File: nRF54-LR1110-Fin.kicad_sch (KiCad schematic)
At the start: 15 parts, among them U1 LR1110IMLTRT, U2 SKY13380-350LF, Y1 TG2520SMN 32.0000M-MCGNNM3, Y2 32.768KHz

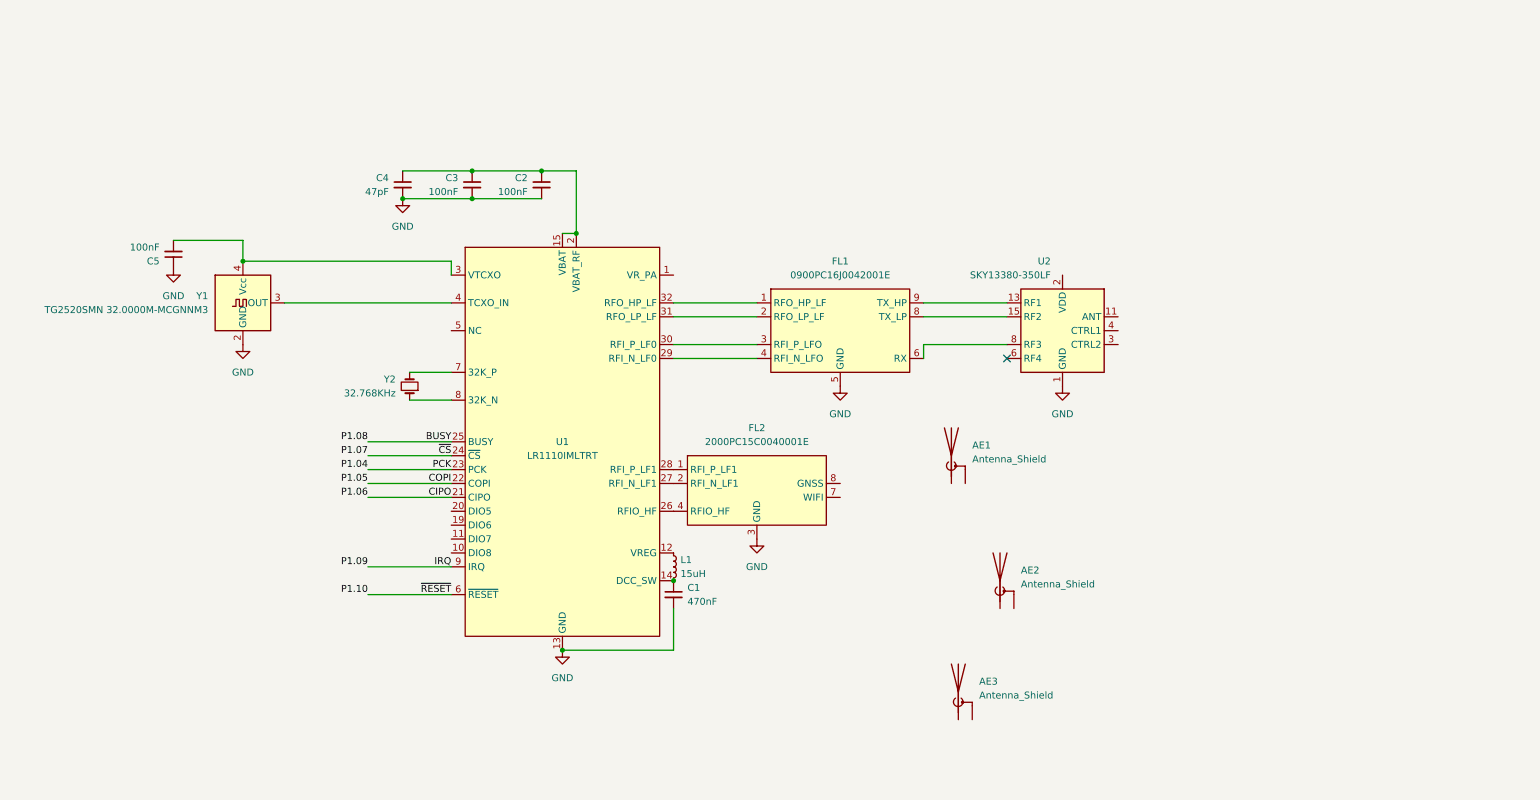
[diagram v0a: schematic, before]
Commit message: schematic: add level shifter, gnss amp
Adds level shifter to L15-DK, GNSS amplifier, proper handling of RF
components for LoRA radio, initial board outline.

Signed-off-by: Helmut Lord <kellyhlord@gmail.com>
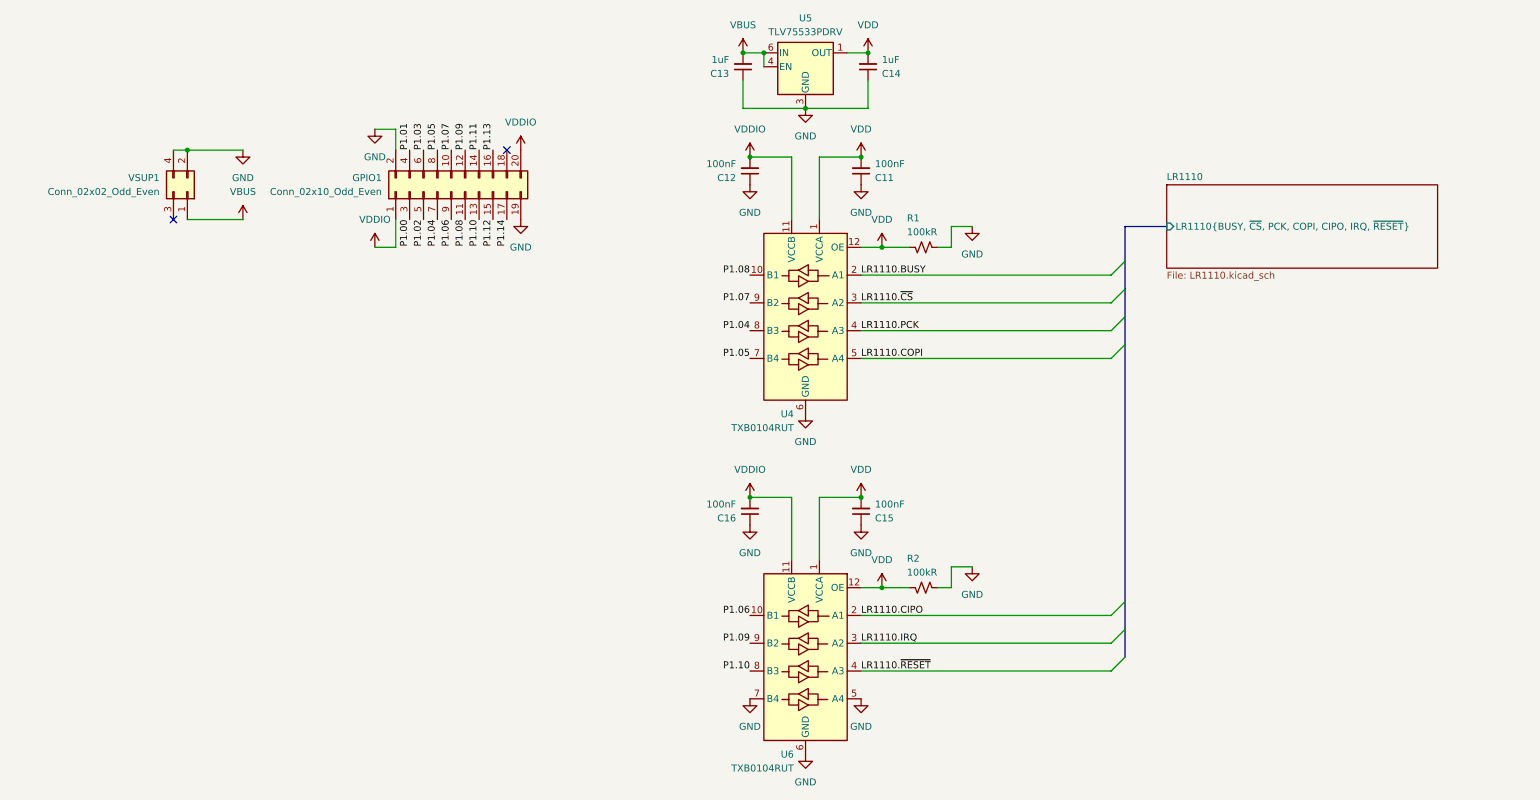
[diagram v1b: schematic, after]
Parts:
- removed AE1, AE2, AE3: Antenna_Shield, Connector_Coaxial:SMA_Amphenol_132289_EdgeMount, symbol Device:Antenna_Shield
- removed C1: 470nF, symbol Device:C_Small
- removed C2, C3, C5: 100nF, symbol Device:C_Small
- removed C4: 47pF, symbol Device:C_Small
- removed FL1: 0900PC16J0042001E, RF_Converter:Balun_Johanson_0900FM15K0039, symbol nRF54-LR1110-Fin-RF:0900PC16J0042001E
- removed FL2: 2000PC15C0040001E, RF_Converter:Balun_Johanson_0900FM15K0039, symbol nRF54-LR1110-Fin-RF:2000PC15C0040001E
- removed L1: 15uH, symbol Device:L_Small
- removed U1: LR1110IMLTRT, Package_DFN_QFN:QFN-32-1EP_5x5mm_P0.5mm_EP3.7x3.7mm_ThermalVias, symbol nRF54-LR1110-Fin-RF:LR1110IMLTRT
- removed U2: SKY13380-350LF, Package_DFN_QFN:QFN-16-1EP_3x3mm_P0.5mm_EP1.7x1.7mm, symbol RF_Switch:SKY13380-350LF
- removed Y1: TG2520SMN 32.0000M-MCGNNM3, Oscillator:Oscillator_SMD_SeikoEpson_TG2520SMN-xxx-xxxxxx-4Pin_2.5x2.0mm, symbol Oscillator:TG2520SMN-xx.xxxxxxMhz-xxxxNM
- removed Y2: 32.768KHz, symbol Device:Crystal_Small
- added C11, C12, C15, C16: 100nF, Capacitor_SMD:C_0402_1005Metric, symbol Device:C_Small
- added C13, C14: 1uF, Capacitor_SMD:C_0402_1005Metric, symbol Device:C_Small
- added GPIO1: Conn_02x10_Odd_Even, Connector_PinSocket_2.54mm:PinSocket_2x10_P2.54mm_Horizontal, symbol Connector_Generic:Conn_02x10_Odd_Even
- added R1, R2: 100kR, Resistor_SMD:R_0402_1005Metric, symbol Device:R_Small_US
- added U4, U6: TXB0104RUT, Package_DFN_QFN:Texas_R-PUQFN-N12, symbol Logic_LevelTranslator:TXB0104RUT
- added U5: TLV75533PDRV, Package_SON:WSON-6-1EP_2x2mm_P0.65mm_EP1x1.6mm_ThermalVias, symbol Regulator_Linear:TLV75533PDRV
- added VSUP1: Conn_02x02_Odd_Even, Connector_PinSocket_2.54mm:PinSocket_2x02_P2.54mm_Horizontal, symbol Connector_Generic:Conn_02x02_Odd_Even
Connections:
- net GND: now also C11.1, C12.1, C13.1, C14.1, C15.1, C16.1, GPIO1.19 (Pin_19), GPIO1.2 (Pin_2), R1.2, R2.2, U4.6 (GND), U5.3 (GND), U5.7 (GND), U6.5 (A4), U6.6 (GND), U6.7 (B4), VSUP1.2 (Pin_2), VSUP1.4 (Pin_4)
- net P1.04: now also GPIO1.7 (Pin_7), U4.8 (B3)
- net P1.07: now also GPIO1.10 (Pin_10), U4.9 (B2)
- net P1.10: now also GPIO1.13 (Pin_13), U6.8 (B3)
- new net LR1110.BUSY: U4.2 (A1)
- new net LR1110.CIPO: U6.2 (A1)
- new net LR1110.COPI: U4.5 (A4)
- new net LR1110.IRQ: U6.3 (A2)
- new net LR1110.PCK: U4.4 (A3)
- new net LR1110.~{CS}: U4.3 (A2)
- new net LR1110.~{RESET}: U6.4 (A3)
- new net P1.00: GPIO1.3 (Pin_3)
- new net P1.01: GPIO1.4 (Pin_4)
- new net P1.02: GPIO1.5 (Pin_5)
- new net P1.03: GPIO1.6 (Pin_6)
- new net P1.05: GPIO1.8 (Pin_8), U4.7 (B4)
- new net P1.06: GPIO1.9 (Pin_9), U6.10 (B1)
- new net P1.08: GPIO1.11 (Pin_11), U4.10 (B1)
- new net P1.09: GPIO1.12 (Pin_12), U6.9 (B2)
- new net P1.11: GPIO1.14 (Pin_14)
- new net P1.12: GPIO1.15 (Pin_15)
- new net P1.13: GPIO1.16 (Pin_16)
- new net P1.14: GPIO1.17 (Pin_17)
- new net VBUS: C13.2, U5.4 (EN), U5.6 (IN), VSUP1.1 (Pin_1)
- new net VDD: C11.2, C14.2, C15.2, R1.1, R2.1, U4.1 (VCCA), U4.12 (OE), U5.1 (OUT), U6.1 (VCCA), U6.12 (OE)
- new net VDDIO: C12.2, C16.2, GPIO1.1 (Pin_1), GPIO1.20 (Pin_20), U4.11 (VCCB), U6.11 (VCCB)
- no-connect marks 1 -> 2
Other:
- added sheet LR1110 (LR1110.kicad_sch)
